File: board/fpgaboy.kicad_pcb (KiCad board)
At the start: 2 copper layers, 50 x 50 mm, 63 parts, among them J1 Conn_01x12, J2 Conn_01x06, J3 Micro_SD_Card_Det, J4 Conn_01x06, P1 ILI9341, P3 USB_OTG, SW1 SWITCH_SPST, U1 iCE40-HX8k-BG121, U2 DSC60XX, U3 GS74116AGP/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

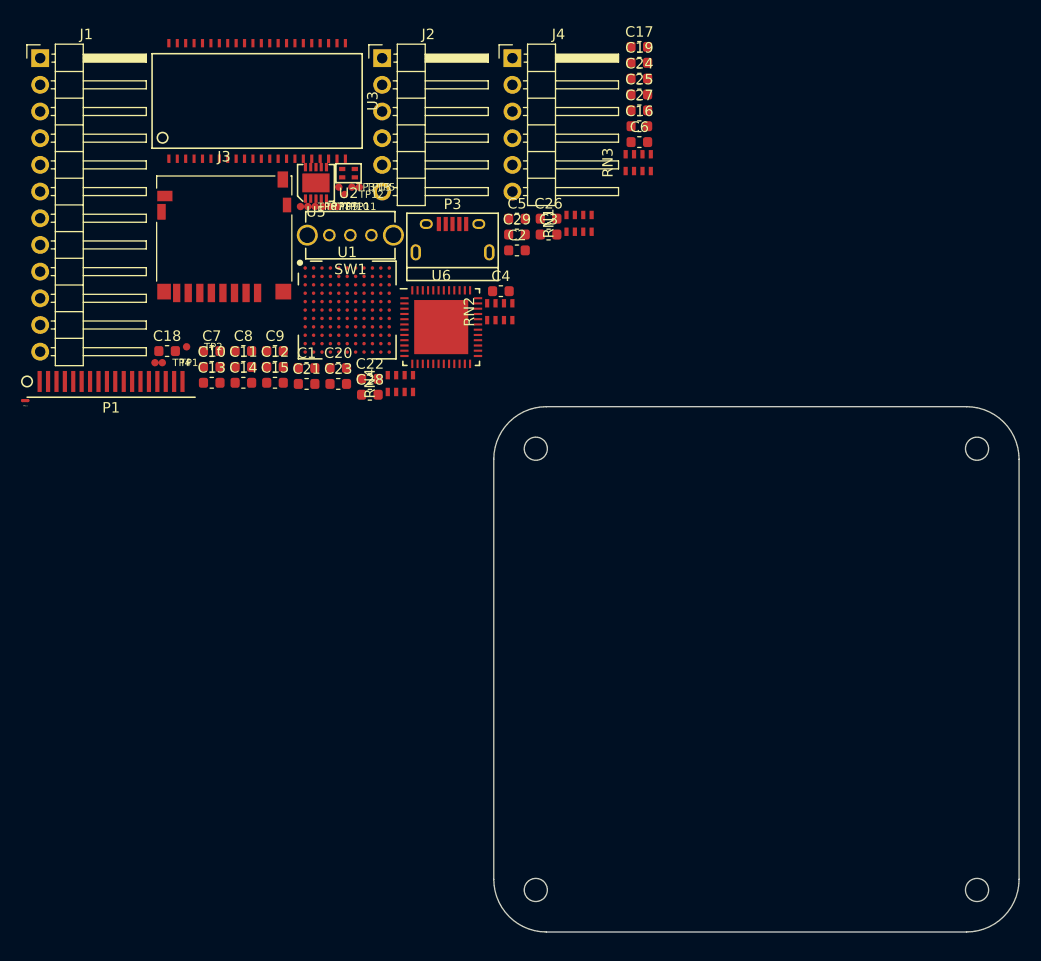
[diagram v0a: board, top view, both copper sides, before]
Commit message: PCB: import netlist, set up board perimeter, planes, DRC.
Former-commit-id: db39540da853fd6e9b11bb7ebc257c05f2c57114 [formerly a41c5352efe3ec2d7d83614421b6e63e598ce97c]
Former-commit-id: a1b8f921a68008d3870cc9ae1145b4fb55359cd4
Former-commit-id: cf0d552804170fee1a25c4142faf7534d85e2960
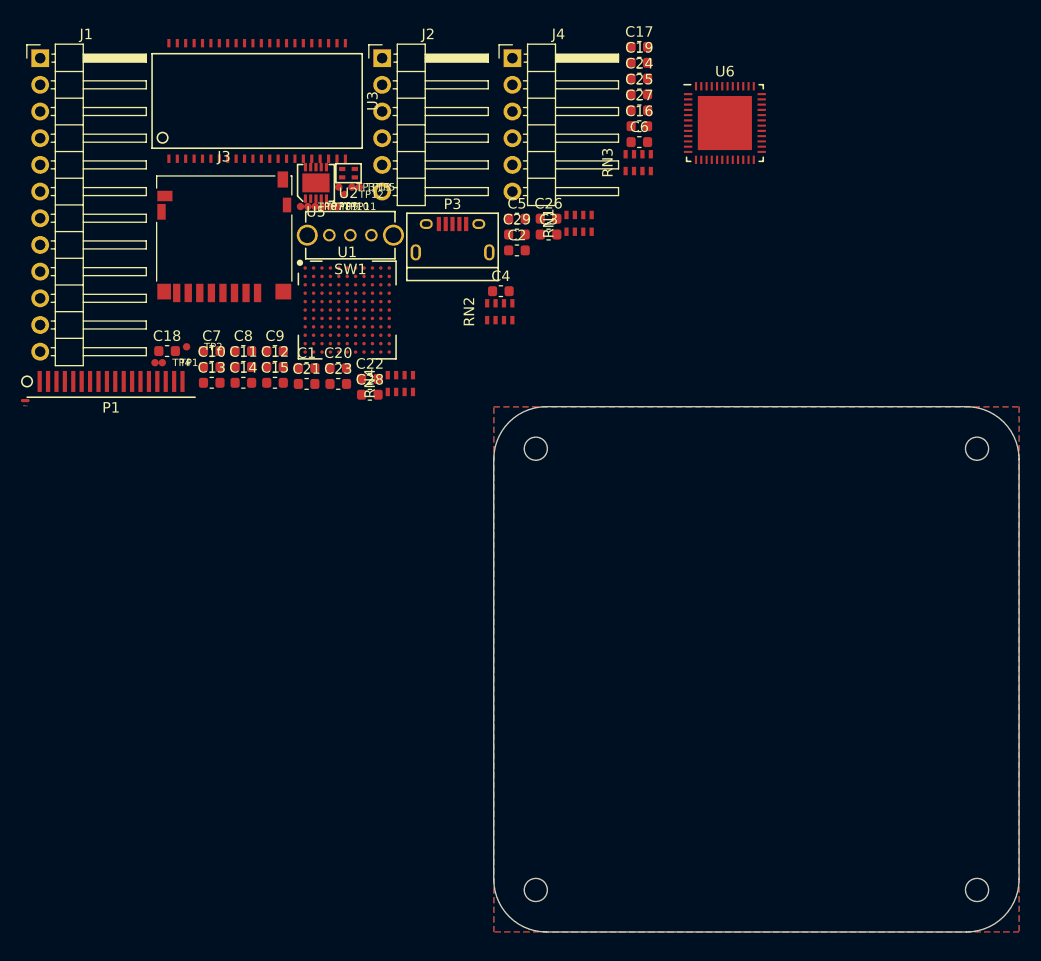
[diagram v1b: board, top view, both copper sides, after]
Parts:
- moved U6 33.3 mm to (152.0, 53.0)
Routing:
- added copper zone on In2.Cu, net +3V3
- added copper zone on B.Cu, net GND
- added copper zone on F.Cu, net GND
- added copper zone on In1.Cu, net GND
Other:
- copper layers 2 -> 4
- net class 0.2 added: clearance 0.15, trace_width 0.2, via_dia 0.6, via_drill 0.3
- net class 0.5 added: clearance 0.2, trace_width 0.5, via_dia 0.7, via_drill 0.4
- net class Default: clearance 0.2 -> 0.15; trace_width 0.25 -> 0.15; via_dia 0.8 -> 0.6; via_drill 0.4 -> 0.3
- rule trace_clearance: 0.2 -> 0.15
- rule trace_min: 0.2 -> 0.15
- rule via_min_size: 0.4 -> 0.6
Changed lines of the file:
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@@
   (layers
     (0 F.Cu signal)
+    (1 In1.Cu power)
+    (2 In2.Cu power)
     (31 B.Cu signal)
     (32 B.Adhes user)
@@
     (46 B.CrtYd user)
     (47 F.CrtYd user)
-    (48 B.Fab user hide)
-    (49 F.Fab user hide)
+    (48 B.Fab user)
+    (49 F.Fab user)
   )
   (setup
-    (last_trace_width 0.25)
-    (trace_clearance 0.2)
-    (zone_clearance 0.508)
-    (zone_45_only no)
-    (trace_min 0.2)
+    (last_trace_width 0.15)
+    (user_trace_width 0.2)
+    (user_trace_width 0.3)
+    (user_trace_width 0.5)
+    (user_trace_width 1)
+    (trace_clearance 0.15)
+    (zone_clearance 0.2)
+    (zone_45_only yes)
+    (trace_min 0.15)
     (segment_width 0.2)
     (edge_width 0.1)
-    (via_size 0.8)
-    (via_drill 0.4)
-    (via_min_size 0.4)
+    (via_size 0.6)
+    (via_drill 0.3)
+    (via_min_size 0.6)
     (via_min_drill 0.3)
     (uvia_size 0.3)
@@
   (net 150 "Net-(U6-Pad48)")
   (net_class Default "This is the default net class."
-    (clearance 0.2)
-    (trace_width 0.25)
-    (via_dia 0.8)
-    (via_drill 0.4)
+    (clearance 0.15)
+    (trace_width 0.15)
+    (via_dia 0.6)
+    (via_drill 0.3)
     (uvia_dia 0.3)
     (uvia_drill 0.1)
@@
     (add_net "Net-(U6-Pad47)")
     (add_net "Net-(U6-Pad48)")
+  )
+  (net_class 0.2 ""
+    (clearance 0.15)
+    (trace_width 0.2)
+    (via_dia 0.6)
+    (via_drill 0.3)
+    (uvia_dia 0.3)
+    (uvia_drill 0.1)
+  )
+  (net_class 0.5 ""
+    (clearance 0.2)
+    (trace_width 0.5)
+    (via_dia 0.7)
+    (via_drill 0.4)
+    (uvia_dia 0.3)
+    (uvia_drill 0.1)
   )
   (module MountingHole:MountingHole_2.2mm_M2_DIN965 (layer F.Cu)
@@
   )
   (module fpgaboy_parts:QFN-48_EP_7x7_Pitch0.5mm (layer F.Cu)
-    (at 124.995001 72.425001)
+    (at 152 53)
     (attr smd)
     (fp_text reference U6 (at 0 -4.9) (layer F.SilkS)
@@
   (gr_arc (start 175 125) (end 175 130) (angle -90) (layer Edge.Cuts) (width 0.1))
   (gr_arc (start 135 125) (end 130 125) (angle -90) (layer Edge.Cuts) (width 0.1))
+  (zone (net 1) (net_name GND) (layer In1.Cu) (hatch edge 0.508)
+    (connect_pads (clearance 0.2))
+    (min_thickness 0.2)
+    (fill (arc_segments 16) (thermal_gap 0.25) (thermal_bridge_width 0.25))
+    (polygon
+      (pts
+        (xy 130 80) (xy 180 80) (xy 180 130) (xy 130 130)
+      )
+    )
+  )
+  (zone (net 1) (net_name GND) (layer F.Cu) (hatch edge 0.508)
+    (connect_pads (clearance 0.2))
+    (min_thickness 0.2)
+    (fill (arc_segments 16) (thermal_gap 0.25) (thermal_bridge_width 0.25))
+    (polygon
+      (pts
+        (xy 130 80) (xy 180 80) (xy 180 130) (xy 130 130)
+      )
+    )
+  )
+  (zone (net 1) (net_name GND) (layer B.Cu) (hatch edge 0.508)
+    (connect_pads (clearance 0.2))
+    (min_thickness 0.2)
+    (fill (arc_segments 16) (thermal_gap 0.25) (thermal_bridge_width 0.25))
+    (polygon
+      (pts
+        (xy 130 80) (xy 180 80) (xy 180 130) (xy 130 130)
+      )
+    )
+  )
+  (zone (net 2) (net_name +3V3) (layer In2.Cu) (hatch edge 0.508)
+    (connect_pads (clearance 0.2))
+    (min_thickness 0.2)
+    (fill (arc_segments 16) (thermal_gap 0.25) (thermal_bridge_width 0.25))
+    (polygon
+      (pts
+        (xy 130 80) (xy 180 80) (xy 180 130) (xy 130 130)
+      )
+    )
+  )
 )

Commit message: Start placing components. Fix references to kicad4 footprints. Alter BGA footprint so that vias can be placed between pads.
Former-commit-id: bd528e47238e1e5486ab4242507cff2d8ebbe877 [formerly e25b043cde048c10d5d4d75b9e60daf800c100f4]
Former-commit-id: 11b4f6d371cc355af72a2cc654ce37b7b2cdccaa
Former-commit-id: 1230468cd22565a20545bb1cbead323269b41e59
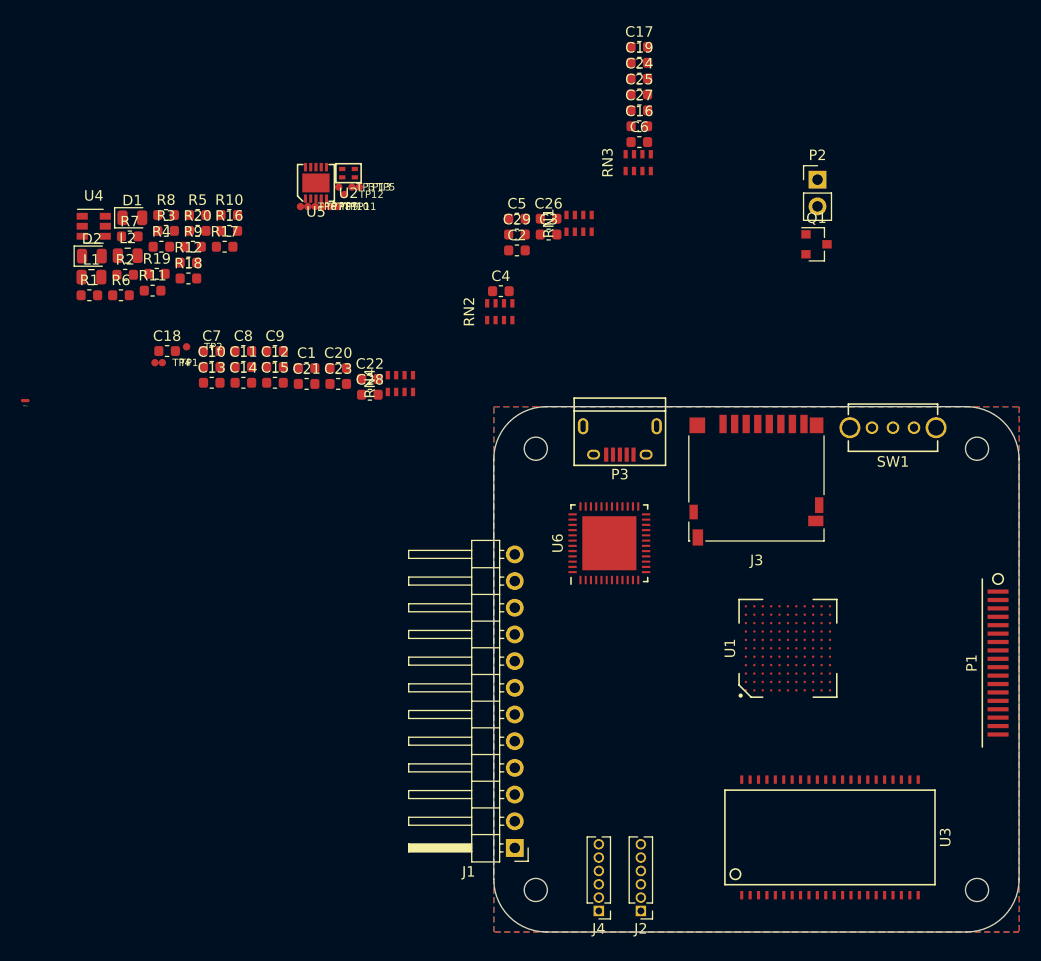
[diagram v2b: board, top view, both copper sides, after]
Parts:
- added D1: LED, LED_SMD:LED_0805_2012Metric, F.Cu at (95.6, 62.0)
- added D2: LED, LED_SMD:LED_0805_2012Metric, F.Cu at (91.7, 65.7)
- added L1: 2u2, Resistor_SMD:R_0805_2012Metric, F.Cu at (91.7, 67.7)
- added L2: 2u2, Resistor_SMD:R_0805_2012Metric, F.Cu at (95.2, 65.6)
- added P2: CONN_01X02, Connector_PinHeader_2.54mm:PinHeader_1x02_P2.54mm_Vertical, F.Cu at (160.8, 58.4)
- added Q1: BSS816NW, Package_TO_SOT_SMD:SOT-23, F.Cu at (160.7, 64.5)
- added R1: 10k, Resistor_SMD:R_0603_1608Metric, F.Cu at (91.5, 69.4)
- added R10: 680, Resistor_SMD:R_0603_1608Metric, F.Cu at (104.8, 61.8)
- added R11: 680, Resistor_SMD:R_0603_1608Metric, F.Cu at (97.5, 69.0)
- added R12: 10k, Resistor_SMD:R_0603_1608Metric, F.Cu at (100.9, 66.3)
- added R16: NF, Resistor_SMD:R_0603_1608Metric, F.Cu at (104.8, 63.3)
- added R17: 450k, Resistor_SMD:R_0603_1608Metric, F.Cu at (104.4, 64.8)
- added R18: 100k, Resistor_SMD:R_0603_1608Metric, F.Cu at (100.9, 67.8)
- added R19: 100k, Resistor_SMD:R_0603_1608Metric, F.Cu at (97.9, 67.4)
- added R2: 220, Resistor_SMD:R_0603_1608Metric, F.Cu at (94.9, 67.4)
- added R20: 100k, Resistor_SMD:R_0603_1608Metric, F.Cu at (101.8, 63.3)
- added R3: 220, Resistor_SMD:R_0603_1608Metric, F.Cu at (98.8, 63.3)
- added R4: 220, Resistor_SMD:R_0603_1608Metric, F.Cu at (98.4, 64.8)
- added R5: 220, Resistor_SMD:R_0603_1608Metric, F.Cu at (101.8, 61.8)
- added R6: 680, Resistor_SMD:R_0603_1608Metric, F.Cu at (94.5, 69.4)
- added R7: 10, Resistor_SMD:R_0603_1608Metric, F.Cu at (95.4, 63.8)
- added R8: 10, Resistor_SMD:R_0603_1608Metric, F.Cu at (98.8, 61.8)
- added R9: 10k, Resistor_SMD:R_0603_1608Metric, F.Cu at (101.4, 64.8)
- added U4: BQ21040, Package_TO_SOT_SMD:SOT-23-6, F.Cu at (91.9, 62.8)
- J2, J4: footprint Connector_PinHeader_2.54mm:PinHeader_1x06_P2.54mm_Horizontal -> Connector_PinHeader_1.27mm:PinHeader_1x06_P1.27mm_Vertical
- moved U3 88.8 mm to (162.0, 121.0)
- moved P1 88.6 mm to (178.0, 104.4), turned to 270 degrees
- moved J1 87.7 mm to (132.0, 122.0), turned to 180 degrees
- moved J2 84.8 mm to (144.0, 128.0), turned to 180 degrees
- moved J4 81.6 mm to (140.0, 128.0), turned to 180 degrees
- moved J3 55.7 mm to (155.0, 87.0), turned to 180 degrees
- moved SW1 54.8 mm to (168.0, 82.0)
- moved U1 52.9 mm to (158.0, 103.0), turned to 90 degrees
- moved U6 41.5 mm to (141.0, 93.0), turned to 90 degrees
- moved P3 24.7 mm to (142.0, 83.0), turned to 180 degrees
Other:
- rule pad_to_mask_clearance: 0 -> 0.1

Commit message: Part placement for switchmode supply. Remove silkscreen on pad in BGA footprint.
Former-commit-id: 3a3be8eab7c0b08d64aa998ecce77922e7b7b81f [formerly 3ca67d1ac3340a2e648bb178ad1a65c83304dd27]
Former-commit-id: 5b3b48003e4daa74b0e82a3c52147ad53126a4d0
Former-commit-id: 2e4ec40682e333392ab8fb2fd83839f39101e2cb
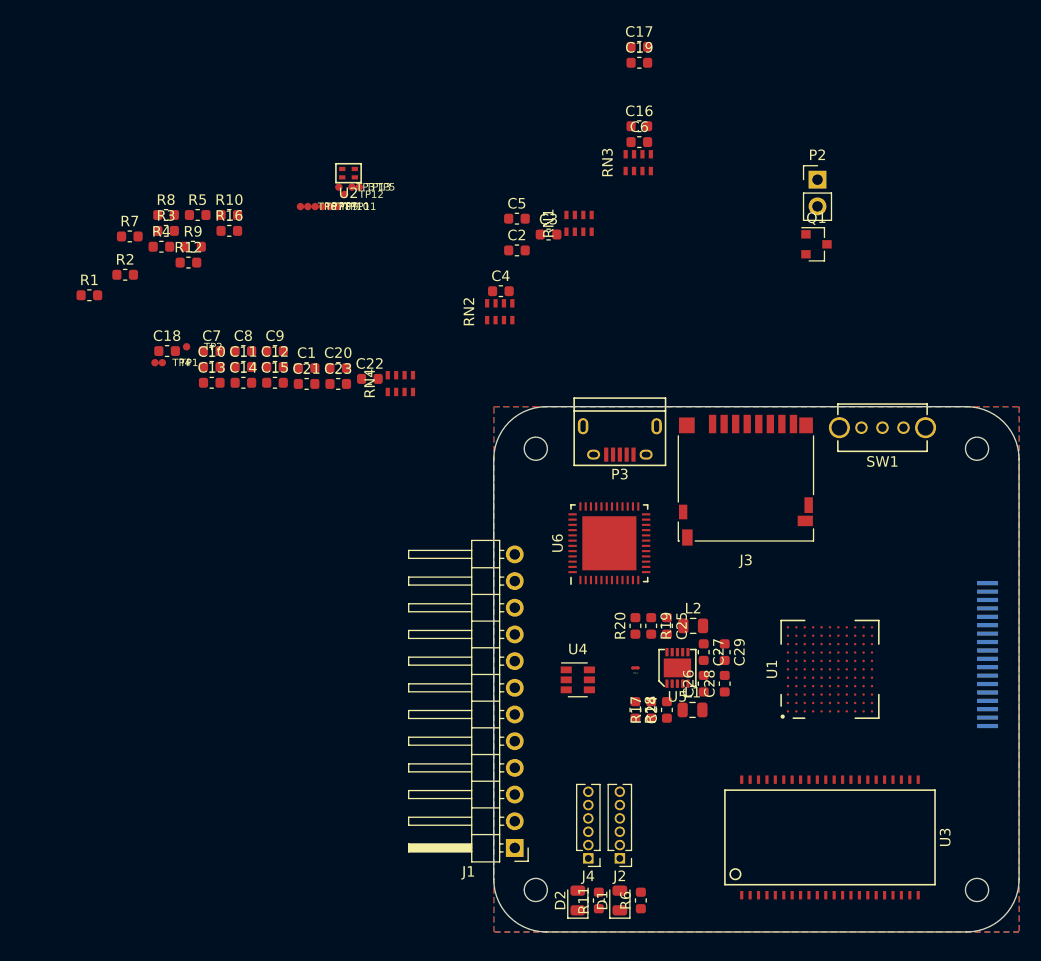
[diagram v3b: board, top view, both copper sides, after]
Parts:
- P1: moved to B.Cu
- moved D1 79.8 mm to (142.0, 127.0), turned to 90 degrees
- moved D2 76.8 mm to (138.0, 127.0), turned to 90 degrees
- moved R6 75.9 mm to (144.0, 127.0), turned to 90 degrees
- moved R11 71.9 mm to (140.0, 127.0), turned to 90 degrees
- moved L1 70.5 mm to (148.9, 108.9)
- moved L2 64.3 mm to (149.0, 100.9)
- moved TP14 63.4 mm to (143.5, 104.9)
- moved U4 63.1 mm to (138.0, 106.0)
- moved C24 60.1 mm to (146.5, 108.9), turned to 90 degrees
- moved R17 59.9 mm to (145.0, 108.9), turned to 90 degrees
- moved R18 59.1 mm to (143.5, 108.9), turned to 270 degrees
- moved R19 57.8 mm to (145.0, 100.9), turned to 270 degrees
- moved U5 57.6 mm to (147.5, 104.9)
- moved R20 56.1 mm to (143.5, 100.9), turned to 90 degrees
- moved C27 51.9 mm to (150.0, 103.4), turned to 270 degrees
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
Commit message: First pass of placing all components.
Former-commit-id: 935330e139bbc688dd3075af15c022303e23c6e1 [formerly f9cef177abd4ecc2c663cb08782e3e3e737b028e]
Former-commit-id: 80bf02931e0e868b70c2aba9824d08be8d3d2d28
Former-commit-id: 687b3f498758089015909bee82d7bb9f30404761
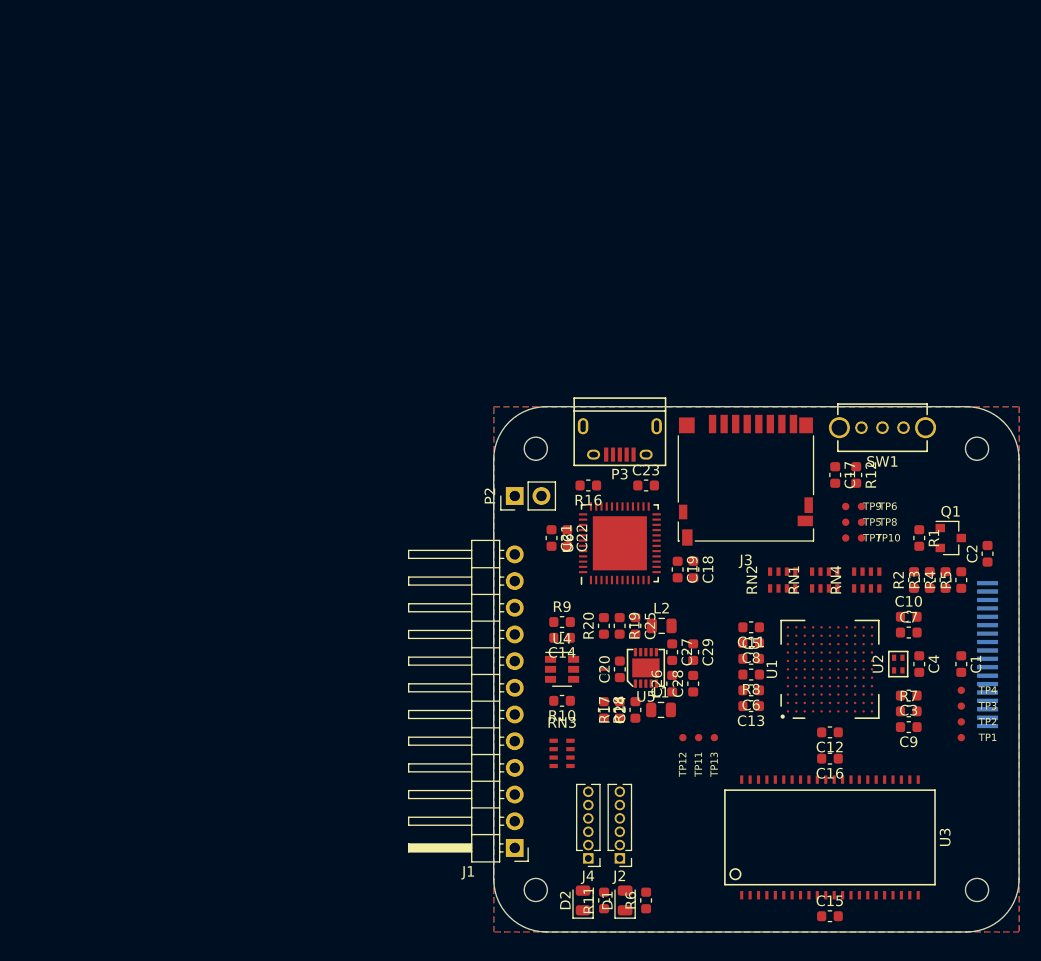
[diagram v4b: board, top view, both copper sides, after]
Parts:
- moved R7 86.8 mm to (169.5, 109.0)
- moved TP1 84.0 mm to (174.5, 111.5)
- moved TP4 82.8 mm to (174.5, 107.0)
- moved R1 82.3 mm to (170.5, 92.5), turned to 270 degrees
- moved TP2 81.9 mm to (174.5, 110.0)
- moved R4 81.1 mm to (173.0, 96.5), turned to 90 degrees
- moved R5 80.6 mm to (174.5, 96.5), turned to 90 degrees
- moved R2 80.5 mm to (170.0, 96.5), turned to 90 degrees
- moved R3 79.9 mm to (171.5, 96.5), turned to 90 degrees
- moved TP3 77.1 mm to (174.5, 108.5)
- moved C15 73.3 mm to (162.0, 128.5)
- moved C7 71.6 mm to (169.5, 101.5)
- moved R8 70.8 mm to (154.5, 105.5), turned to 180 degrees
- moved C10 70.5 mm to (169.5, 100.0)
- moved U2 70.2 mm to (168.5, 104.5), turned to 270 degrees
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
